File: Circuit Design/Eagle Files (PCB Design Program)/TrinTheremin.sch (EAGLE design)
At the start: 50 parts, among them T1 FDN340P/PMV48XP, T2 PMV48XP, T3 PBSS4360Z, T4 PBSS4360Z, Y2 16MHz KX-7

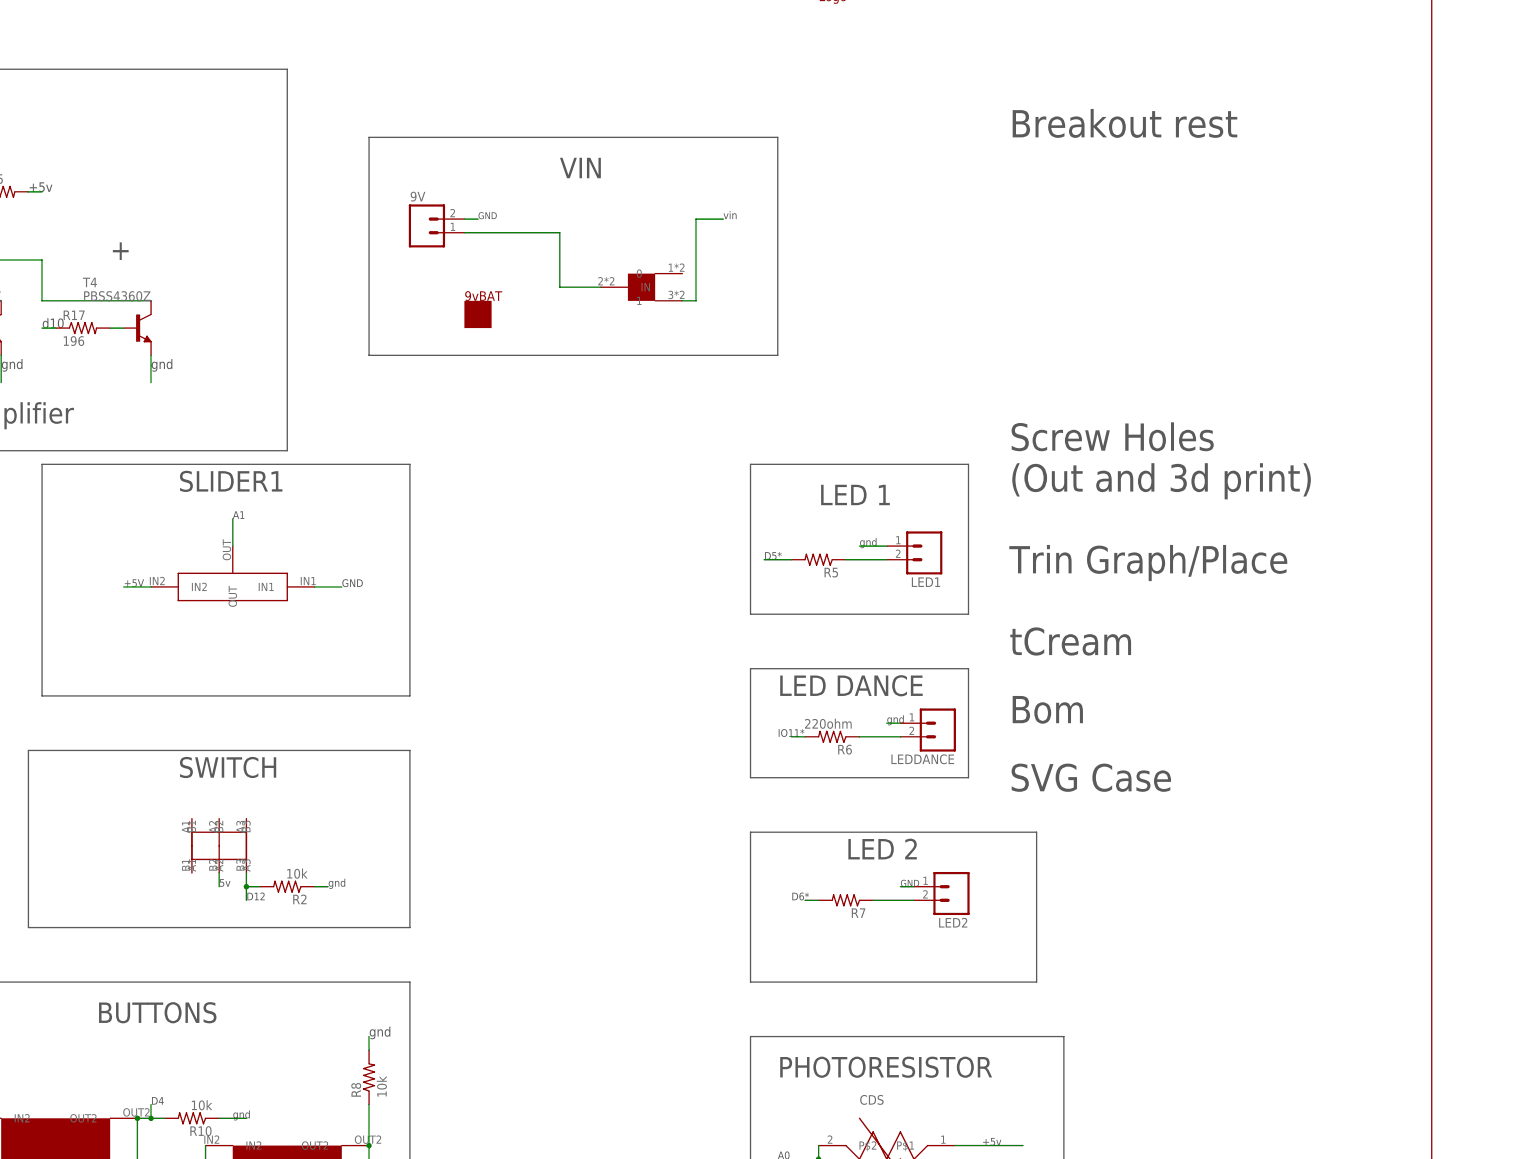
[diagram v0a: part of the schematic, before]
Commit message: Misc. Changes... see details
Added circuit design pictures, fixed horn (reversed), changed solidworks
files to display PCB below part, added datasheet (in progress), changed
folder names, reorganized
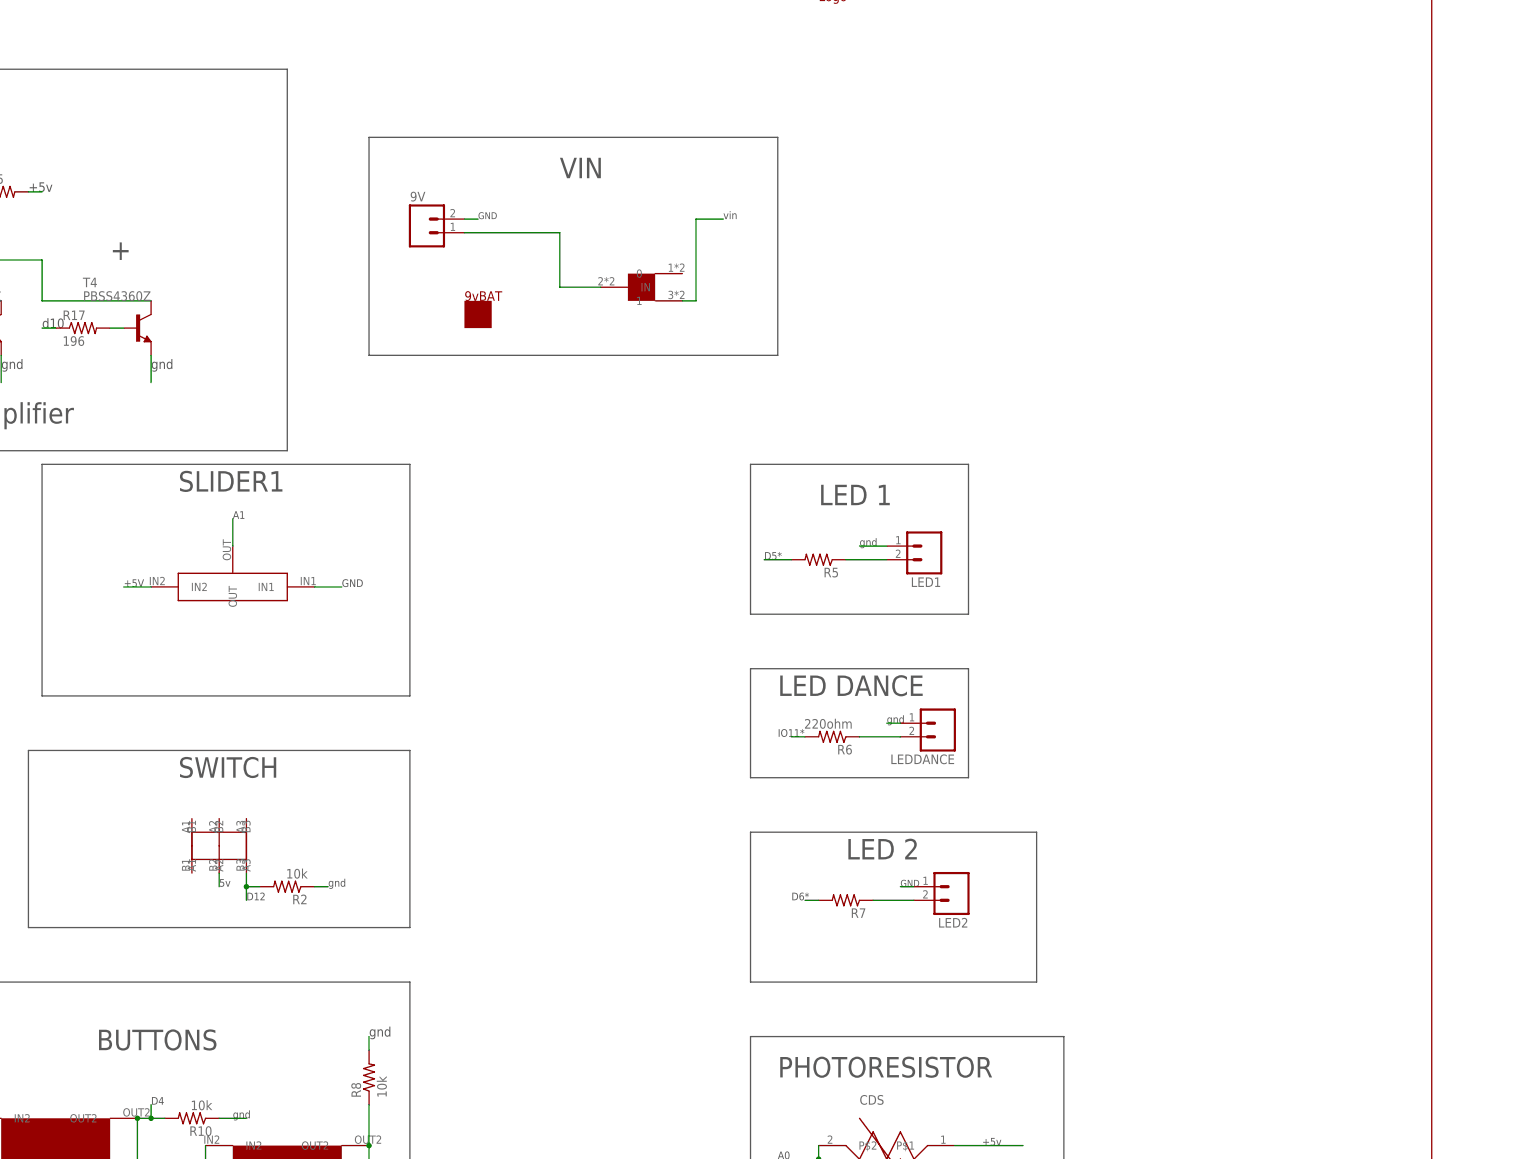
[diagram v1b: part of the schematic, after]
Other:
- note removed: "Bom"
- note removed: "Breakout rest"
- note removed: "SVG Case"
- note removed: "Screw Holes (Out and 3d print)"
- note removed: "Trin Graph/Place"
- note removed: "tCream"
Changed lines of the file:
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@@
 <?xml version="1.0" encoding="utf-8"?>
 <!DOCTYPE eagle SYSTEM "eagle.dtd">
-<eagle version="8.2.0">
+<eagle version="7.6.0">
 <drawing>
 <settings>
@@
 <wire x1="162.56" y1="-78.74" x2="162.56" y2="-30.48" width="0.1524" layer="97"/>
 <wire x1="162.56" y1="-30.48" x2="63.5" y2="-30.48" width="0.1524" layer="97"/>
-<text x="104.14" y="-38.1" size="3.81" layer="97">BUTTONS
+<text x="104.14" y="-43.18" size="3.81" layer="97">BUTTONS
 </text>
 <wire x1="93.98" y1="66.04" x2="93.98" y2="22.86" width="0.1524" layer="97"/>
@@
 <text x="132.08" y="-15.24" size="1.4224" layer="97">D12</text>
 <text x="114.3" y="-53.34" size="1.4224" layer="97">D4</text>
-<text x="274.32" y="127" size="5.08" layer="97">Breakout rest</text>
-<text x="274.32" y="60.96" size="5.08" layer="97">Screw Holes
-(Out and 3d print)</text>
-<text x="274.32" y="45.72" size="5.08" layer="97">Trin Graph/Place</text>
-<text x="274.32" y="30.48" size="5.08" layer="97">tCream</text>
-<text x="274.32" y="17.78" size="5.08" layer="97">Bom</text>
-<text x="274.32" y="5.08" size="5.08" layer="97">SVG Case</text>
 <text x="-30.48" y="86.36" size="1.778" layer="97">gnd</text>
 <text x="-30.48" y="86.36" size="1.778" layer="97">gnd</text>
